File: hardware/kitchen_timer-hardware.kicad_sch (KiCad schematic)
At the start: 0 parts

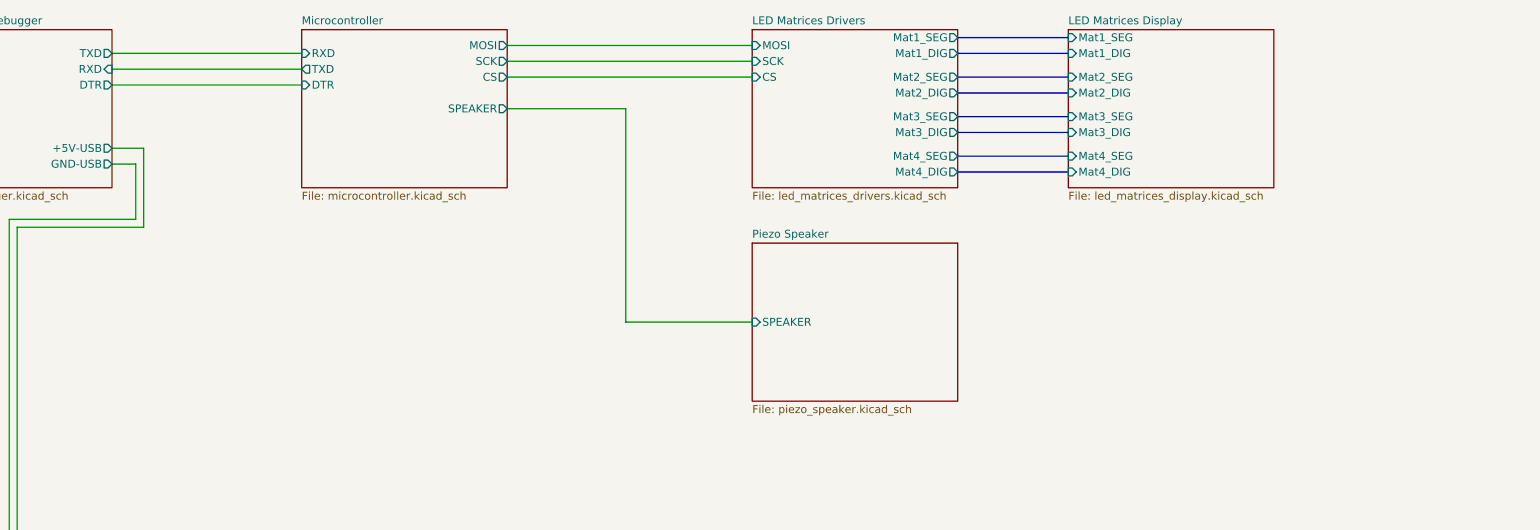
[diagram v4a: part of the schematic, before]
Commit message: Added components to the UART Module to prevent backfeeding the module when the USB is not connected.
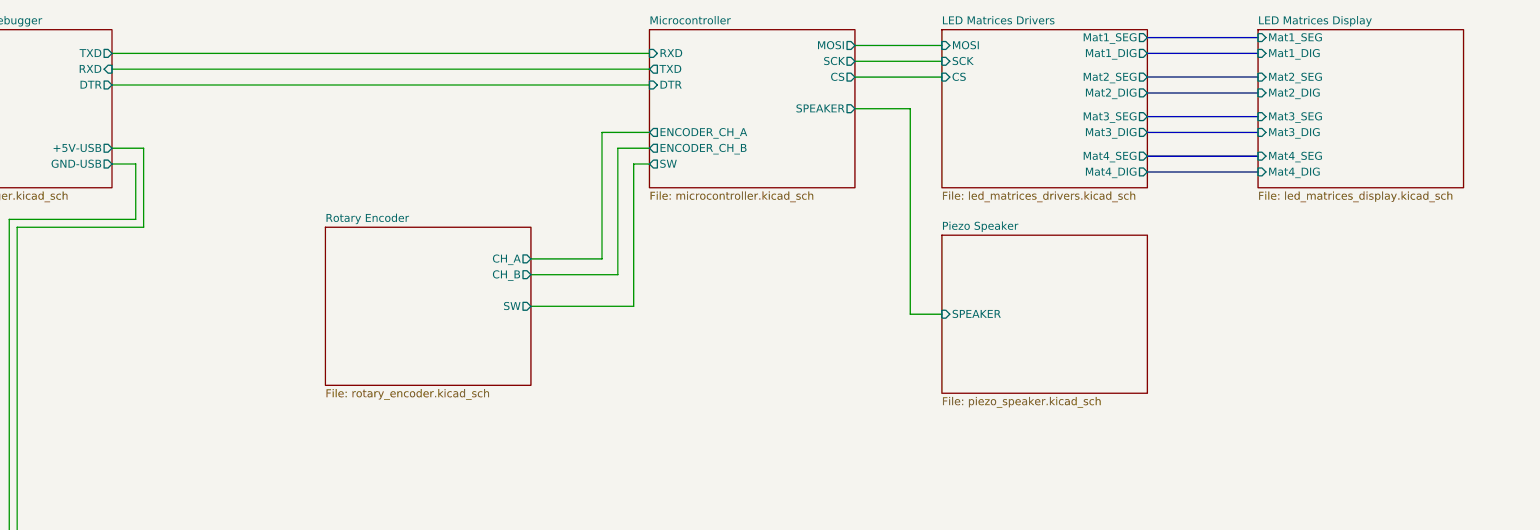
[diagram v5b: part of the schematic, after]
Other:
- added sheet Rotary Encoder (rotary_encoder.kicad_sch)
- sheet Microcontroller ports: added ENCODER_CH_A, ENCODER_CH_B, SW; removed none

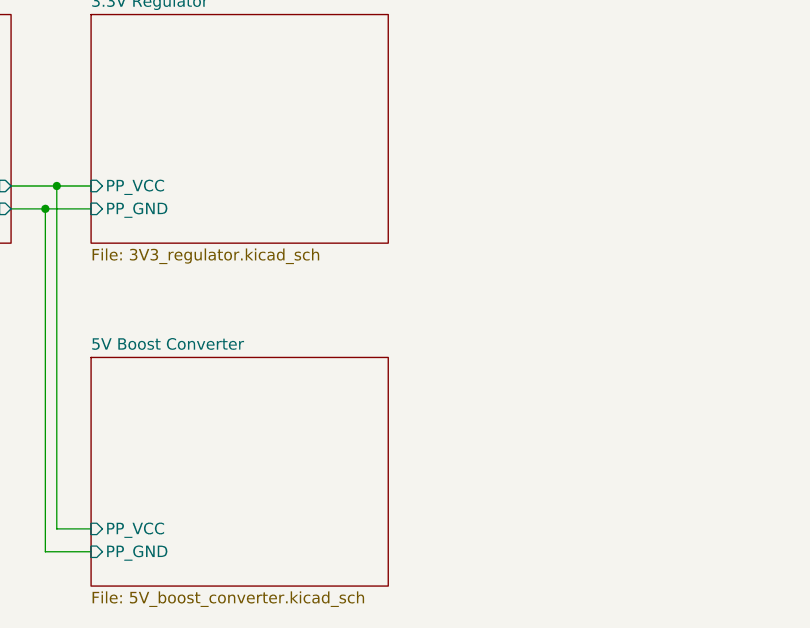
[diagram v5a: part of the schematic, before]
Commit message: Made the global labels for power visible in the main shchematic
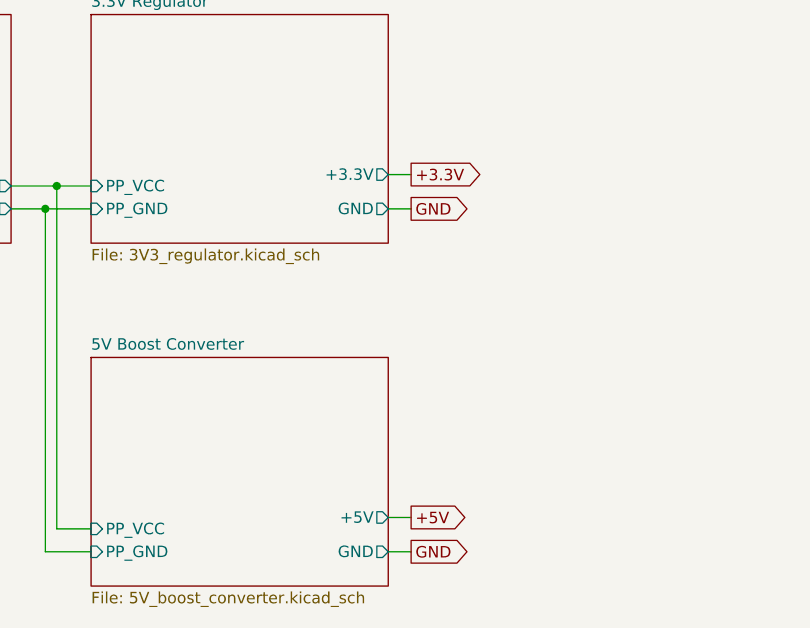
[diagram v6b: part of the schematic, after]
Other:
- sheet 3.3V Regulator ports: added +3.3V, GND; removed none
- sheet 5V Boost Converter ports: added +5V, GND; removed none
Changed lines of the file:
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@@
+	(wire
+		(pts
+			(xy 120.65 173.99) (xy 123.19 173.99)
+		)
+		(stroke
+			(width 0)
+			(type default)
+		)
+	)
 	(wire
 		(pts
@@
 	(wire
 		(pts
+			(xy 120.65 170.18) (xy 123.19 170.18)
+		)
+		(stroke
+			(width 0)
+			(type default)
+		)
+	)
+	(wire
+		(pts
 			(xy 58.42 31.75) (xy 144.78 31.75)
 		)
@@
 	(wire
 		(pts
+			(xy 120.65 135.89) (xy 123.19 135.89)
+		)
+		(stroke
+			(width 0)
+			(type default)
+		)
+	)
+	(wire
+		(pts
 			(xy 142.24 46.99) (xy 144.78 46.99)
 		)
@@
 	(wire
 		(pts
+			(xy 120.65 132.08) (xy 123.19 132.08)
+		)
+		(stroke
+			(width 0)
+			(type default)
+		)
+	)
+	(wire
+		(pts
 			(xy 177.8 38.1) (xy 186.69 38.1)
 		)
@@
 			(width 0)
 			(type default)
+		)
+	)
+	(global_label "+5V"
+		(shape output)
+		(at 123.19 170.18 0)
+		(fields_autoplaced yes)
+		(effects
+			(font
+				(size 1.27 1.27)
+			)
+			(justify left)
+		)
+		(property "Intersheetrefs" "${INTERSHEET_REFS}"
+			(at 130.0457 170.18 0)
+			(effects
+				(font
+					(size 1.27 1.27)
+				)
+				(justify left)
+				(hide yes)
+			)
+		)
+	)
+	(global_label "+3.3V"
+		(shape output)
+		(at 123.19 132.08 0)
+		(fields_autoplaced yes)
+		(effects
+			(font
+				(size 1.27 1.27)
+			)
+			(justify left)
+		)
+		(property "Intersheetrefs" "${INTERSHEET_REFS}"
+			(at 131.86 132.08 0)
+			(effects
+				(font
+					(size 1.27 1.27)
+				)
+				(justify left)
+				(hide yes)
+			)
+		)
+	)
+	(global_label "GND"
+		(shape output)
+		(at 123.19 135.89 0)
+		(fields_autoplaced yes)
+		(effects
+			(font
+				(size 1.27 1.27)
+			)
+			(justify left)
+		)
+		(property "Intersheetrefs" "${INTERSHEET_REFS}"
+			(at 130.0457 135.89 0)
+			(effects
+				(font
+					(size 1.27 1.27)
+				)
+				(justify left)
+				(hide yes)
+			)
+		)
+	)
+	(global_label "GND"
+		(shape output)
+		(at 123.19 173.99 0)
+		(fields_autoplaced yes)
+		(effects
+			(font
+				(size 1.27 1.27)
+			)
+			(justify left)
+		)
+		(property "Intersheetrefs" "${INTERSHEET_REFS}"
+			(at 130.0457 173.99 0)
+			(effects
+				(font
+					(size 1.27 1.27)
+				)
+				(justify left)
+				(hide yes)
+			)
 		)
 	)
@@
 			)
 		)
+		(pin "GND" output
+			(at 120.65 173.99 0)
+			(effects
+				(font
+					(size 1.27 1.27)
+				)
+				(justify right)
+			)
+		)
+		(pin "+5V" output
+			(at 120.65 170.18 0)
+			(effects
+				(font
+					(size 1.27 1.27)
+				)
+				(justify right)
+			)
+		)
 		(instances
 			(project "kitchen_timer-hardware"
@@
 			)
 		)
+		(pin "+3.3V" output
+			(at 120.65 132.08 0)
+			(effects
+				(font
+					(size 1.27 1.27)
+				)
+				(justify right)
+			)
+		)
+		(pin "GND" output
+			(at 120.65 135.89 0)
+			(effects
+				(font
+					(size 1.27 1.27)
+				)
+				(justify right)
+			)
+		)

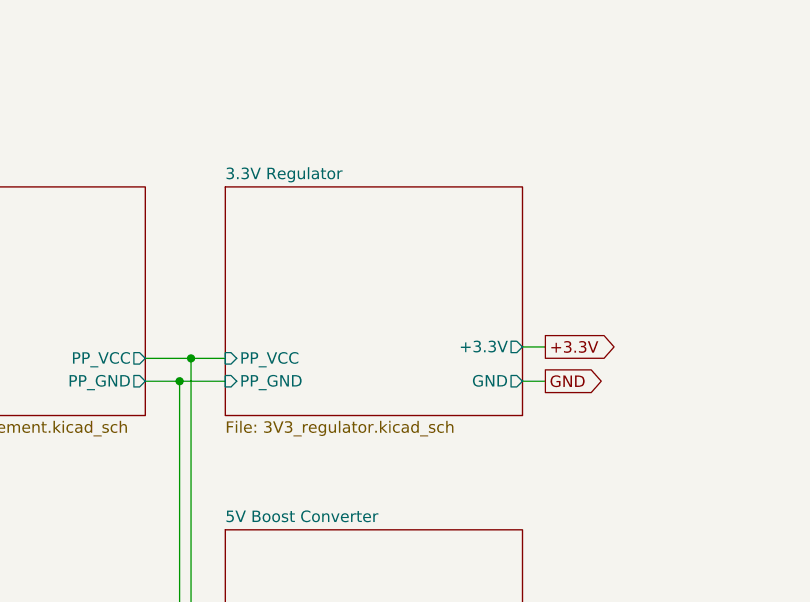
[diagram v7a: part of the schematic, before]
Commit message: Removed the 3.3V Regulator since we might need to run everything out of 5V
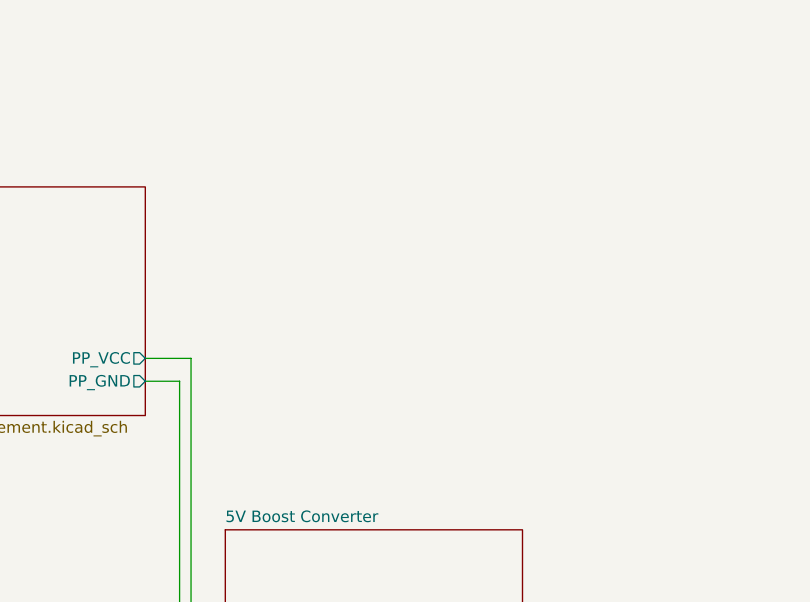
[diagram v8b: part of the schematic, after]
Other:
- removed sheet 3.3V Regulator
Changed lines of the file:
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@@
 		(comment 4 "Author: Nicolas Perozzi")
 	)
-	(junction
-		(at 82.55 135.89)
-		(diameter 0)
-		(color 0 0 0 0)
-	)
-	(junction
-		(at 83.82 133.35)
-		(diameter 0)
-		(color 0 0 0 0)
-	)
 	(bus
 		(pts
@@
 	(wire
 		(pts
-			(xy 82.55 135.89) (xy 87.63 135.89)
-		)
-		(stroke
-			(width 0)
-			(type default)
-		)
-	)
-	(wire
-		(pts
 			(xy 58.42 44.45) (xy 63.5 44.45)
 		)
@@
 	(wire
 		(pts
-			(xy 120.65 135.89) (xy 123.19 135.89)
-		)
-		(stroke
-			(width 0)
-			(type default)
-		)
-	)
-	(wire
-		(pts
 			(xy 142.24 46.99) (xy 144.78 46.99)
 		)
@@
 	(wire
 		(pts
-			(xy 120.65 132.08) (xy 123.19 132.08)
-		)
-		(stroke
-			(width 0)
-			(type default)
-		)
-	)
-	(wire
-		(pts
 			(xy 177.8 38.1) (xy 186.69 38.1)
 		)
@@
 		(pts
 			(xy 137.16 41.91) (xy 144.78 41.91)
-		)
-		(stroke
-			(width 0)
-			(type default)
-		)
-	)
-	(wire
-		(pts
-			(xy 83.82 133.35) (xy 87.63 133.35)
 		)
 		(stroke
@@
 		)
 	)
-	(global_label "+3.3V"
-		(shape output)
-		(at 123.19 132.08 0)
-		(fields_autoplaced yes)
-		(effects
-			(font
-				(size 1.27 1.27)
-			)
-			(justify left)
-		)
-		(property "Intersheetrefs" "${INTERSHEET_REFS}"
-			(at 131.86 132.08 0)
-			(effects
-				(font
-					(size 1.27 1.27)
-				)
-				(justify left)
-				(hide yes)
-			)
-		)
-	)
-	(global_label "GND"
-		(shape output)
-		(at 123.19 135.89 0)
-		(fields_autoplaced yes)
-		(effects
-			(font
-				(size 1.27 1.27)
-			)
-			(justify left)
-		)
-		(property "Intersheetrefs" "${INTERSHEET_REFS}"
-			(at 130.0457 135.89 0)
-			(effects
-				(font
-					(size 1.27 1.27)
-				)
-				(justify left)
-				(hide yes)
-			)
-		)
-	)
 	(global_label "GND"
 		(shape output)
@@
 				)
 			)
-		)
-	)
-	(sheet
-		(at 87.63 114.3)
-		(size 33.02 25.4)
-		(fields_autoplaced yes)
-		(stroke
-			(width 0.1524)
-			(type solid)
-		)
-		(fill
-			(color 0 0 0 0.0000)
-		)
-		(property "Sheetname" "3.3V Regulator"
-			(at 87.63 113.5884 0)
-			(effects
-				(font
-					(size 1.27 1.27)
-				)
-				(justify left bottom)
-			)
-		)
-		(property "Sheetfile" "3V3_regulator.kicad_sch"
-			(at 87.63 140.2846 0)
-			(effects
-				(font
-					(size 1.27 1.27)
-				)
-				(justify left top)
-			)
-		)
-		(pin "PP_VCC" input
-			(at 87.63 133.35 180)
-			(effects
-				(font
-					(size 1.27 1.27)
-				)
-				(justify left)
-			)
-		)
-		(pin "PP_GND" input
-			(at 87.63 135.89 180)
-			(effects
-				(font
-					(size 1.27 1.27)
-				)
-				(justify left)
-			)
-		)
-		(pin "+3.3V" output
-			(at 120.65 132.08 0)
-			(effects
-				(font
-					(size 1.27 1.27)
-				)
-				(justify right)
-			)
-		)
-		(pin "GND" output
-			(at 120.65 135.89 0)
-			(effects
-				(font
-					(size 1.27 1.27)
-				)
-				(justify right)
-			)
-		)
-		(instances
-			(project "kitchen_timer-hardware"
-				(path "/8963deea-96bc-4401-b671-98fbe9ed9c6a"
-					(page "4")
-				)
-			)
